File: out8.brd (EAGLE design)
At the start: 100 x 80 mm, 38 parts, among them IC1 74HC595N, K301 S202S02, K302 S202S02, K303 S202S02, K304 S202S02, K305 S202S02, K306 S202S02, K307 S202S02, K308 S202S02

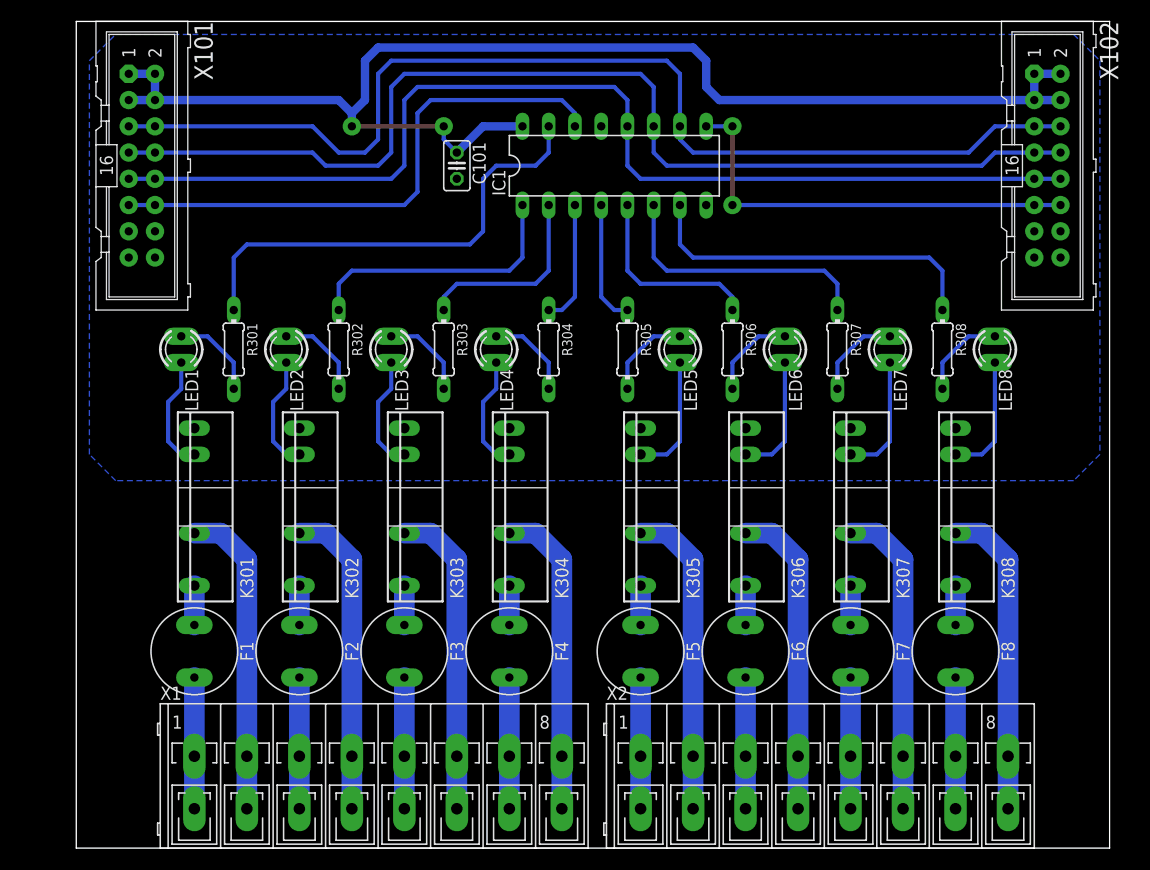
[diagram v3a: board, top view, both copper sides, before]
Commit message: Werte im Schema und Bohrungen im Layout hinzugefügt
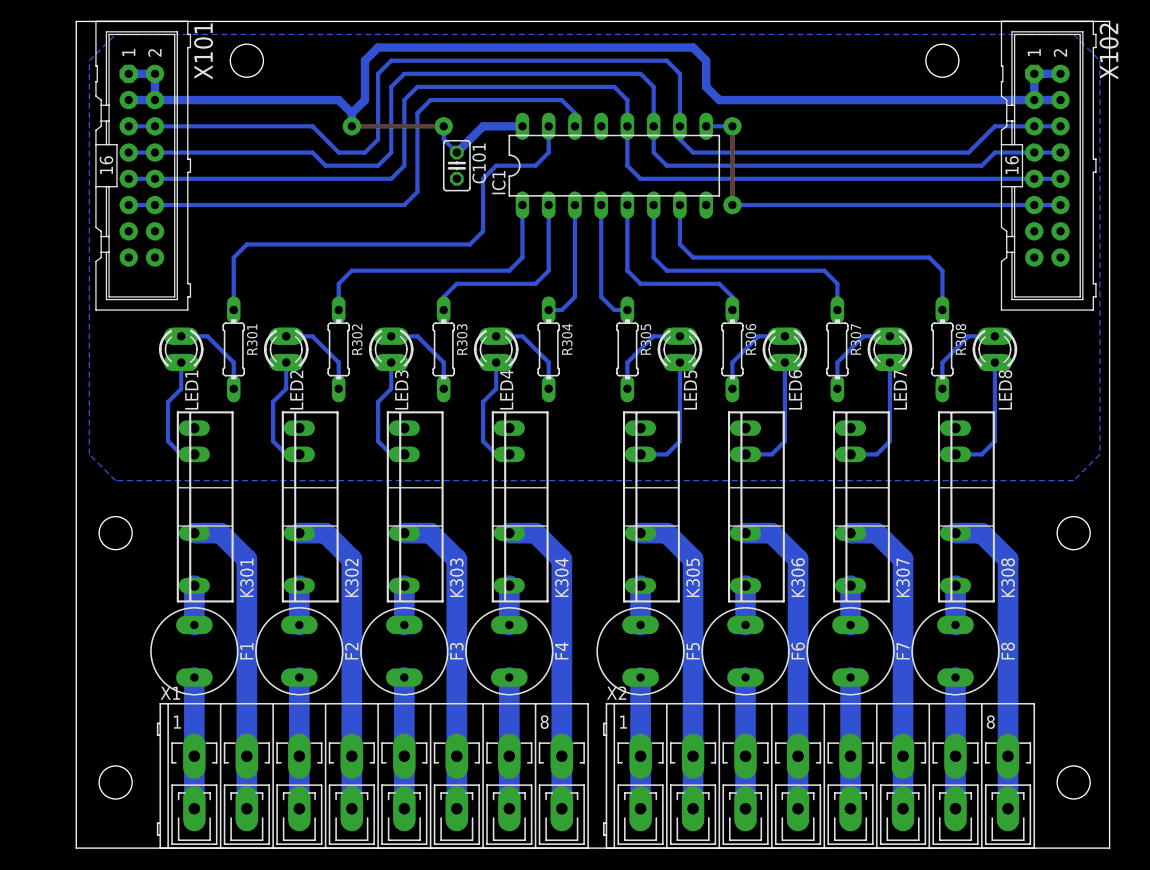
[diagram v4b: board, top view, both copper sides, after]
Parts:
- C101: value 10nF -> 100nF
- F1, F2, F3, F4, F5, F6, F7, F8: value (none) -> 2T
- R301, R302, R303, R304, R305, R306, R307, R308: value (none) -> 180Ω
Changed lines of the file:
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@@
 <layer number="43" name="vRestrict" color="2" fill="10" visible="yes" active="yes"/>
 <layer number="44" name="Drills" color="7" fill="1" visible="no" active="yes"/>
-<layer number="45" name="Holes" color="7" fill="1" visible="no" active="yes"/>
+<layer number="45" name="Holes" color="7" fill="1" visible="yes" active="yes"/>
 <layer number="46" name="Milling" color="3" fill="1" visible="no" active="yes"/>
 <layer number="47" name="Measures" color="7" fill="1" visible="no" active="yes"/>
@@
 <wire x1="100" y1="80" x2="0" y2="80" width="0" layer="20"/>
 <wire x1="0" y1="80" x2="0" y2="0" width="0" layer="20"/>
+<hole x="16.51" y="76.2" drill="3.2"/>
+<hole x="83.82" y="76.2" drill="3.2"/>
+<hole x="3.81" y="6.35" drill="3.2"/>
+<hole x="96.52" y="6.35" drill="3.2"/>
+<hole x="3.81" y="30.48" drill="3.2"/>
+<hole x="96.52" y="30.48" drill="3.2"/>
 </plain>
 <attributes>
@@
 <attribute name="VDRM" value="600" x="142.24" y="55.88" size="1.778" layer="27" rot="R90" display="off"/>
 </element>
-<element name="R301" library="passiv" package="0204/7" value="" x="15.24" y="48.26" rot="R270"/>
-<element name="R302" library="passiv" package="0204/7" value="" x="25.4" y="48.26" rot="R270"/>
-<element name="R303" library="passiv" package="0204/7" value="" x="35.56" y="48.26" rot="R270"/>
-<element name="R304" library="passiv" package="0204/7" value="" x="45.72" y="48.26" rot="R270"/>
-<element name="R305" library="passiv" package="0204/7" value="" x="53.34" y="48.26" rot="R270"/>
-<element name="R306" library="passiv" package="0204/7" value="" x="63.5" y="48.26" rot="R270"/>
-<element name="R307" library="passiv" package="0204/7" value="" x="73.66" y="48.26" rot="R270"/>
-<element name="R308" library="passiv" package="0204/7" value="" x="83.82" y="48.26" rot="R270"/>
-<element name="C101" library="passiv" package="C025-025X050" value="10nF" x="36.83" y="66.04" rot="R270"/>
-<element name="F1" library="sicherung" package="TR5" value="" x="11.43" y="19.05" rot="R270">
+<element name="R301" library="passiv" package="0204/7" value="180Ω" x="15.24" y="48.26" rot="R270"/>
+<element name="R302" library="passiv" package="0204/7" value="180Ω" x="25.4" y="48.26" rot="R270"/>
+<element name="R303" library="passiv" package="0204/7" value="180Ω" x="35.56" y="48.26" rot="R270"/>
+<element name="R304" library="passiv" package="0204/7" value="180Ω" x="45.72" y="48.26" rot="R270"/>
+<element name="R305" library="passiv" package="0204/7" value="180Ω" x="53.34" y="48.26" rot="R270"/>
+<element name="R306" library="passiv" package="0204/7" value="180Ω" x="63.5" y="48.26" rot="R270"/>
+<element name="R307" library="passiv" package="0204/7" value="180Ω" x="73.66" y="48.26" rot="R270"/>
+<element name="R308" library="passiv" package="0204/7" value="180Ω" x="83.82" y="48.26" rot="R270"/>
+<element name="C101" library="passiv" package="C025-025X050" value="100nF" x="36.83" y="66.04" rot="R270"/>
+<element name="F1" library="sicherung" package="TR5" value="2T" x="11.43" y="19.05" rot="R270">
 <attribute name="OC_NEWARK" value="unknown" x="11.43" y="19.05" size="1.778" layer="27" rot="R270" display="off"/>
 <attribute name="MPN" value="" x="11.43" y="19.05" size="1.778" layer="27" rot="R270" display="off"/>
@@
 <attribute name="OC_FARNELL" value="unknown" x="11.43" y="19.05" size="1.778" layer="27" rot="R270" display="off"/>
 </element>
-<element name="F2" library="sicherung" package="TR5" value="" x="21.59" y="19.05" rot="R270">
+<element name="F2" library="sicherung" package="TR5" value="2T" x="21.59" y="19.05" rot="R270">
 <attribute name="OC_NEWARK" value="unknown" x="21.59" y="19.05" size="1.778" layer="27" rot="R270" display="off"/>
 <attribute name="MPN" value="" x="21.59" y="19.05" size="1.778" layer="27" rot="R270" display="off"/>
@@
 <attribute name="OC_FARNELL" value="unknown" x="21.59" y="19.05" size="1.778" layer="27" rot="R270" display="off"/>
 </element>
-<element name="F3" library="sicherung" package="TR5" value="" x="31.75" y="19.05" rot="R270">
+<element name="F3" library="sicherung" package="TR5" value="2T" x="31.75" y="19.05" rot="R270">
 <attribute name="OC_NEWARK" value="unknown" x="31.75" y="19.05" size="1.778" layer="27" rot="R270" display="off"/>
 <attribute name="MPN" value="" x="31.75" y="19.05" size="1.778" layer="27" rot="R270" display="off"/>
@@
 <attribute name="OC_FARNELL" value="unknown" x="31.75" y="19.05" size="1.778" layer="27" rot="R270" display="off"/>
 </element>
-<element name="F4" library="sicherung" package="TR5" value="" x="41.91" y="19.05" rot="R270">
+<element name="F4" library="sicherung" package="TR5" value="2T" x="41.91" y="19.05" rot="R270">
 <attribute name="OC_NEWARK" value="unknown" x="41.91" y="19.05" size="1.778" layer="27" rot="R270" display="off"/>
 <attribute name="MPN" value="" x="41.91" y="19.05" size="1.778" layer="27" rot="R270" display="off"/>
@@
 <attribute name="OC_FARNELL" value="unknown" x="41.91" y="19.05" size="1.778" layer="27" rot="R270" display="off"/>
 </element>
-<element name="F5" library="sicherung" package="TR5" value="" x="54.61" y="19.05" rot="R270">
+<element name="F5" library="sicherung" package="TR5" value="2T" x="54.61" y="19.05" rot="R270">
 <attribute name="OC_NEWARK" value="unknown" x="54.61" y="19.05" size="1.778" layer="27" rot="R270" display="off"/>
 <attribute name="MPN" value="" x="54.61" y="19.05" size="1.778" layer="27" rot="R270" display="off"/>
@@
 <attribute name="OC_FARNELL" value="unknown" x="54.61" y="19.05" size="1.778" layer="27" rot="R270" display="off"/>
 </element>
-<element name="F6" library="sicherung" package="TR5" value="" x="64.77" y="19.05" rot="R270">
+<element name="F6" library="sicherung" package="TR5" value="2T" x="64.77" y="19.05" rot="R270">
 <attribute name="OC_NEWARK" value="unknown" x="64.77" y="19.05" size="1.778" layer="27" rot="R270" display="off"/>
 <attribute name="MPN" value="" x="64.77" y="19.05" size="1.778" layer="27" rot="R270" display="off"/>
@@
 <attribute name="OC_FARNELL" value="unknown" x="64.77" y="19.05" size="1.778" layer="27" rot="R270" display="off"/>
 </element>
-<element name="F7" library="sicherung" package="TR5" value="" x="74.93" y="19.05" rot="R270">
+<element name="F7" library="sicherung" package="TR5" value="2T" x="74.93" y="19.05" rot="R270">
 <attribute name="OC_NEWARK" value="unknown" x="74.93" y="19.05" size="1.778" layer="27" rot="R270" display="off"/>
 <attribute name="MPN" value="" x="74.93" y="19.05" size="1.778" layer="27" rot="R270" display="off"/>
@@
 <attribute name="OC_FARNELL" value="unknown" x="74.93" y="19.05" size="1.778" layer="27" rot="R270" display="off"/>
 </element>
-<element name="F8" library="sicherung" package="TR5" value="" x="85.09" y="19.05" rot="R270">
+<element name="F8" library="sicherung" package="TR5" value="2T" x="85.09" y="19.05" rot="R270">
 <attribute name="OC_NEWARK" value="unknown" x="85.09" y="19.05" size="1.778" layer="27" rot="R270" display="off"/>
 <attribute name="MPN" value="" x="85.09" y="19.05" size="1.778" layer="27" rot="R270" display="off"/>

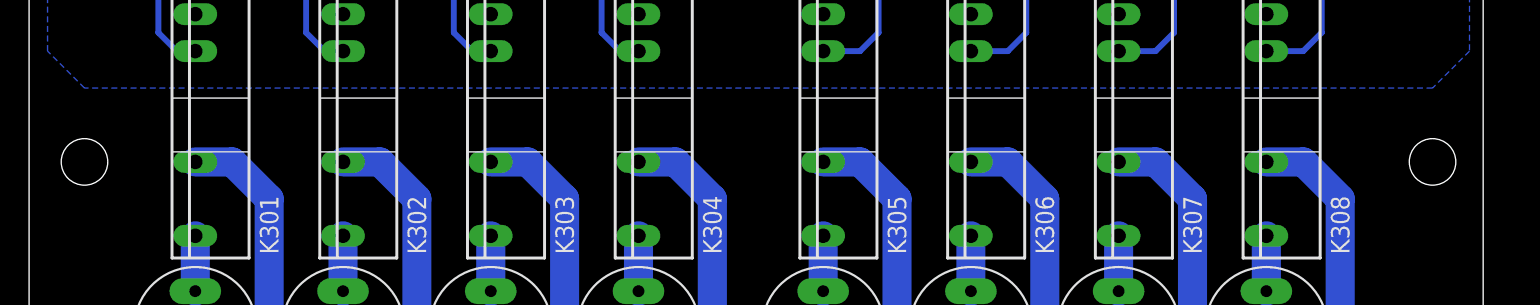
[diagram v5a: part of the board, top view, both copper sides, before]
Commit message: Optionaler Abschlusswiderstand eingefügt
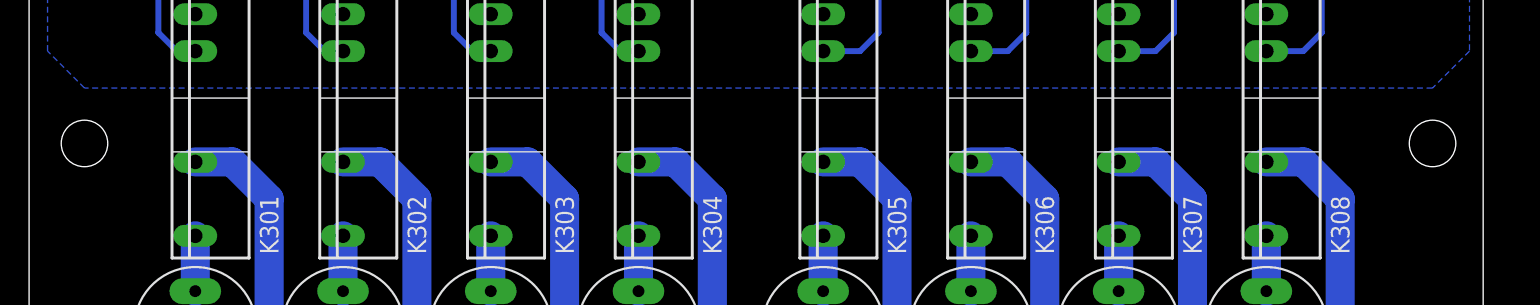
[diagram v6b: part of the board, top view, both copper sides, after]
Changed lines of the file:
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@@
 <hole x="3.81" y="6.35" drill="3.2"/>
 <hole x="96.52" y="6.35" drill="3.2"/>
-<hole x="3.81" y="30.48" drill="3.2"/>
-<hole x="96.52" y="30.48" drill="3.2"/>
+<hole x="3.81" y="31.75" drill="3.2"/>
+<hole x="96.52" y="31.75" drill="3.2"/>
 </plain>
 <attributes>
